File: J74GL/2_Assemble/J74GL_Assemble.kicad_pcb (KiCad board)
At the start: 2 copper layers, 305.2 x 99.2 mm, 223 parts, among them J1 Conn_01x02, SW1 SW_PUSH, SW10 SW_PUSH, SW11 SW_PUSH, SW12 SW_PUSH, SW13 SW_PUSH, SW14 SW_PUSH, SW15 SW_PUSH, SW16 SW_PUSH, SW17 SW_PUSH, SW18 SW_PUSH, SW19 SW_PUSH, SW2 KEY_SWITCH, SW2 SW_PUSH, SW20 SW_PUSH, SW21 SW_PUSH, SW22 SW_PUSH, SW23 SW_PUSH, SW24 SW_PUSH, SW25 SW_PUSH, SW26 SW_PUSH, SW27 SW_PUSH, SW28 SW_PUSH, SW29 SW_PUSH, SW3 SW_PUSH, SW30 SW_PUSH, SW31 SW_PUSH, SW32 SW_PUSH, SW33 SW_PUSH, SW34 SW_PUSH, SW35 SW_PUSH, SW36 SW_PUSH, SW37 SW_PUSH, SW38 SW_PUSH, SW39 SW_PUSH, SW4 SW_PUSH, SW40 SW_PUSH, SW41 SW_PUSH, SW42 SW_PUSH, SW43 SW_PUSH, SW44 SW_PUSH, SW45 SW_PUSH, SW46 SW_PUSH, SW47 SW_PUSH, SW48 SW_PUSH, SW49 SW_PUSH, SW5 SW_PUSH, SW50 SW_PUSH, SW51 SW_PUSH, SW52 SW_PUSH, SW53 SW_PUSH, SW54 SW_PUSH, SW55 SW_PUSH, SW56 SW_PUSH, SW57 SW_PUSH, SW58 SW_PUSH, SW59 SW_PUSH, SW6 SW_PUSH, SW60 SW_PUSH, SW61 SW_PUSH, SW62 SW_PUSH, SW63 SW_PUSH, SW64 SW_PUSH, SW65 SW_PUSH, SW66 SW_PUSH, SW67 SW_PUSH, SW68 SW_PUSH, SW69 SW_PUSH, SW7 SW_PUSH, SW70 SW_PUSH, SW71 SW_PUSH, SW72 SW_PUSH, SW73 SW_PUSH, SW74 SW_PUSH, SW8 SW_PUSH, SW9 SW_PUSH, U1 BLEMicroPro

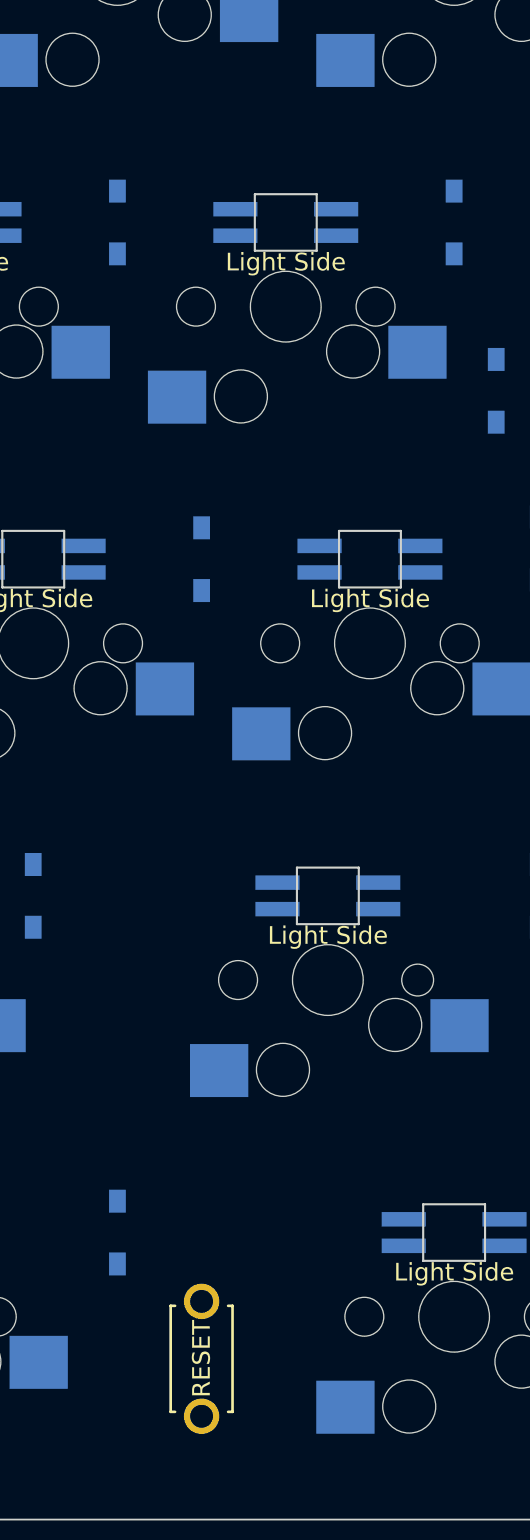
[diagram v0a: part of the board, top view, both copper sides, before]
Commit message: バックプレートとボトムプレートの追加
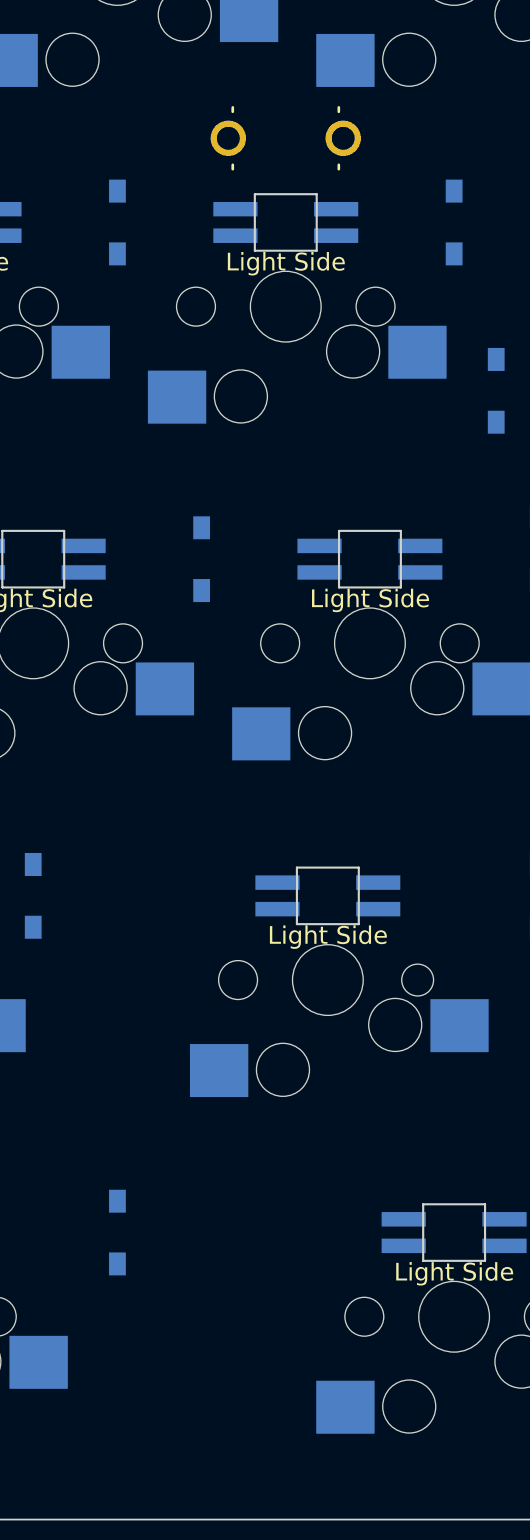
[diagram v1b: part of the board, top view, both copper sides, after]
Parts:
- SW74: moved to B.Cu
- moved SW74 69.2 mm to (266.7, 38.1), turned to 180 degrees
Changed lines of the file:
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@@
     (pad "" np_thru_hole circle (at -11.938 -6.985 90) (size 3.048 3.048) (drill 3.048) (layers *.Cu *.Mask))
   )
-  (module kbd:ResetSW_FL (layer F.Cu)
-    (at 261.9375 107.15625 90)
-    (fp_text reference SW74 (at 0 2.55 90) (layer F.SilkS) hide
-      (effects (font (size 1 1) (thickness 0.15)))
+  (module kbd:ResetSW_FL (layer B.Cu)
+    (at 266.7 38.1 180)
+    (fp_text reference SW74 (at 0 -2.55) (layer B.SilkS) hide
+      (effects (font (size 1 1) (thickness 0.15)) (justify mirror))
     )
-    (fp_text value SW_PUSH (at 0 -2.55 90) (layer F.Fab)
-      (effects (font (size 1 1) (thickness 0.15)))
+    (fp_text value SW_PUSH (at 0 2.55) (layer B.Fab)
+      (effects (font (size 1 1) (thickness 0.15)) (justify mirror))
     )
-    (fp_text user RESET (at 0 0 90) (layer F.SilkS)
-      (effects (font (size 1 1) (thickness 0.15)))
+    (fp_text user RESET (at 0 0) (layer B.SilkS)
+      (effects (font (size 1 1) (thickness 0.15)) (justify mirror))
     )
-    (fp_line (start 3 -1.75) (end 3 -1.5) (layer F.SilkS) (width 0.15))
-    (fp_line (start -3 -1.75) (end 3 -1.75) (layer F.SilkS) (width 0.15))
+    (fp_line (start 3 1.75) (end 3 1.5) (layer B.SilkS) (width 0.15))
+    (fp_line (start -3 1.75) (end 3 1.75) (layer B.SilkS) (width 0.15))
+    (fp_line (start -3 1.75) (end -3 1.5) (layer B.SilkS) (width 0.15))
+    (fp_line (start -3 -1.75) (end -3 -1.5) (layer B.SilkS) (width 0.15))
+    (fp_line (start 3 -1.75) (end 3 -1.5) (layer B.SilkS) (width 0.15))
+    (fp_line (start -3 -1.75) (end 3 -1.75) (layer B.SilkS) (width 0.15))
+    (fp_line (start 3 1.75) (end 3 1.5) (layer F.SilkS) (width 0.15))
+    (fp_line (start -3 1.5) (end -3 1.75) (layer F.SilkS) (width 0.15))
     (fp_line (start -3 -1.75) (end -3 -1.5) (layer F.SilkS) (width 0.15))
-    (fp_line (start -3 1.75) (end -3 1.5) (layer F.SilkS) (width 0.15))
-    (fp_line (start 3 1.75) (end 3 1.5) (layer F.SilkS) (width 0.15))
-    (fp_line (start -3 1.75) (end 3 1.75) (layer F.SilkS) (width 0.15))
-    (fp_line (start 3 -1.75) (end 3 -1.5) (layer B.SilkS) (width 0.15))
-    (fp_line (start -3 -1.5) (end -3 -1.75) (layer B.SilkS) (width 0.15))
-    (fp_line (start -3 1.75) (end -3 1.5) (layer B.SilkS) (width 0.15))
-    (fp_line (start 3 1.5) (end 3 1.75) (layer B.SilkS) (width 0.15))
-    (pad 2 thru_hole circle (at -3.25 0 90) (size 2 2) (drill 1.3) (layers *.Cu *.Mask F.SilkS)
+    (fp_line (start 3 -1.5) (end 3 -1.75) (layer F.SilkS) (width 0.15))
+    (pad 2 thru_hole circle (at -3.25 0 180) (size 2 2) (drill 1.3) (layers *.Cu *.Mask B.SilkS)
       (net 79 GND))
-    (pad 1 thru_hole circle (at 3.25 0 90) (size 2 2) (drill 1.3) (layers *.Cu *.Mask F.SilkS)
+    (pad 1 thru_hole circle (at 3.25 0 180) (size 2 2) (drill 1.3) (layers *.Cu *.Mask B.SilkS)
       (net 155 Reset))
   )
